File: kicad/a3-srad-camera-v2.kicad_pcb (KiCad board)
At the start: 4 copper layers, 50 x 50 mm, 162 parts, among them J1 BOARD_IND, J2 OUT, J3 Amphenol F32Q 1x22 P=0.5mm, SW1 PWRON, U1 AMS1117-3.3, U2 TPS6521905RHBR, U3 STM32U575RGT6, U4 RV1106G2

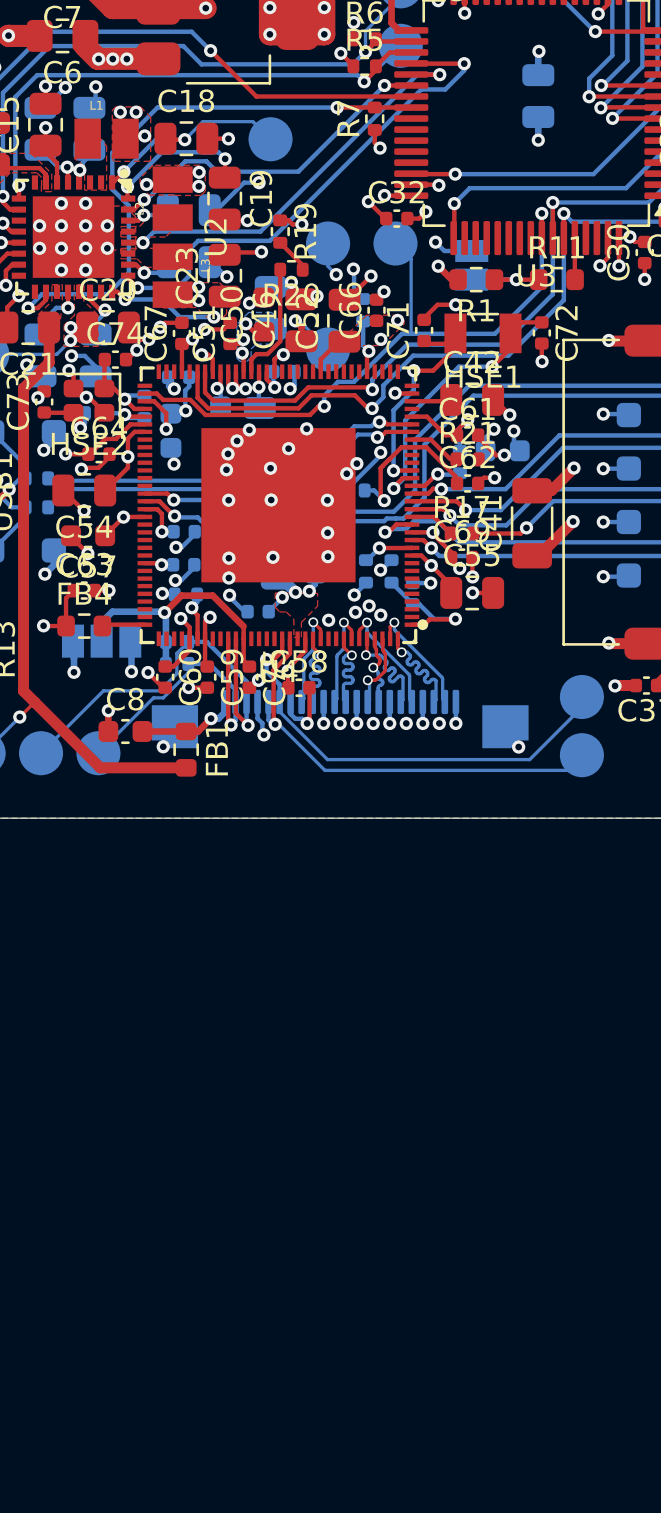
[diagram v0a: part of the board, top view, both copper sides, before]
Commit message: PCB before switching STM32
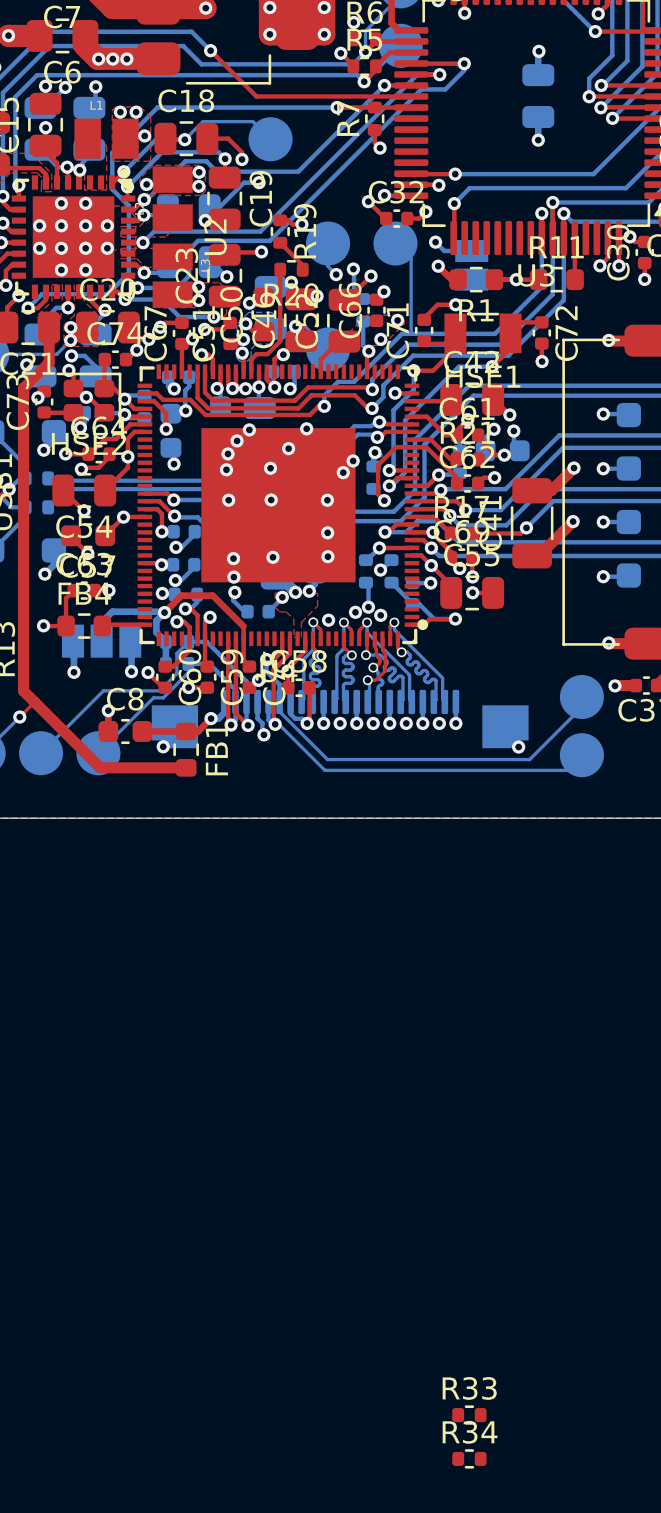
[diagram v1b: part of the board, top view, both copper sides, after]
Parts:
- added R33: DNP, Resistor_SMD:R_0402_1005Metric, F.Cu at (158.0, 153.1)
- added R34: DNP, Resistor_SMD:R_0402_1005Metric, F.Cu at (158.0, 155.1)
- R14, R15: value 22R -> 2.2R
- moved R22 1.08 mm to (153.6, 110.5), turned to 90 degrees
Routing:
- net /VCC_1V8_RK: track 21.8 -> 20.2 mm
- net GND: track 142.7 -> 144.2 mm, vias 158 -> 157
- net Net-(U4A-ETH_EXTR): track 2.22 -> 2.75 mm

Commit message: Add missing passives and microphone
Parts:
- removed the C34 at (159.4, 86.2)
- removed the R21 at (157.9, 109.7)
- added C59: 100nF, Capacitor_SMD:C_0402_1005Metric, F.Cu at (159.3, 109.8)
- added C73: 100nF, Capacitor_SMD:C_0402_1005Metric, B.Cu at (168.3, 101.9)
- added C74: 100nF, Capacitor_SMD:C_0402_1005Metric, B.Cu at (166.7, 101.9)
- added C80: 1uF, Capacitor_SMD:C_0603_1608Metric, F.Cu at (157.6, 102.0)
- added C81: 100nF, Capacitor_SMD:C_0402_1005Metric, F.Cu at (169.4, 99.6)
- added C82: 100pF, Capacitor_SMD:C_0402_1005Metric, B.Cu at (172.3, 101.5)
- added C83: 100pF, Capacitor_SMD:C_0402_1005Metric, B.Cu at (171.3, 100.5)
- added C84: 100pF, Capacitor_SMD:C_0402_1005Metric, B.Cu at (171.3, 102.5)
- added C85: 1uF, Capacitor_SMD:C_0603_1608Metric, F.Cu at (155.3, 101.2)
- added MIC1: IM73A135V01, Sensor_Audio:Infineon_PG-LLGA-5-2, F.Cu at (173.1, 101.5)
- added R19: 10k, Resistor_SMD:R_0603_1608Metric, B.Cu at (136.5, 117.9)
- added R22: 10k, Resistor_SMD:R_0603_1608Metric, B.Cu at (135.0, 117.9)
- added R32: 10k, Resistor_SMD:R_0603_1608Metric, B.Cu at (168.3, 104.4)
- added R33: 10k, Resistor_SMD:R_0603_1608Metric, B.Cu at (166.7, 104.4)
- added R39: 22k, Resistor_SMD:R_0402_1005Metric, F.Cu at (169.5, 101.2)
- added R40: 22k, Resistor_SMD:R_0402_1005Metric, F.Cu at (169.5, 102.1)
- added TP14: TestPoint, a3-srad-camera-v2:TestPoint_Pad_D2.0mm_Small_Courtyard, B.Cu at (170.7, 104.9)
- C38: renamed from C39; moved to B.Cu
- C39: renamed from C40; moved to B.Cu
- C62, R1, R11: moved to B.Cu
- R25: renamed from R33; moved to B.Cu
- R26: renamed from R34; moved to B.Cu
- U3: value STM32U575RGT6 -> STM32U073R8Tx
- moved R26 51.9 mm to (163.8, 103.5), turned to 180 degrees
- moved R25 50.9 mm to (163.8, 102.5), turned to 180 degrees
- moved C39 17.5 mm to (160.2, 117.7)
- moved C38 17.5 mm to (164.0, 117.7)
- moved C62 5.67 mm to (152.2, 111.1), turned to 180 degrees
- moved R11 2.33 mm to (160.2, 100.0), turned to 90 degrees
- moved C65 1.63 mm to (159.8, 107.7)
- moved JP1 0.96 mm to (158.1, 100.0)
- moved C66 0.95 mm to (156.6, 104.5), turned to -90 degrees
- moved C61 0.90 mm to (157.3, 107.9)
- moved R27 0.83 mm to (156.7, 109.6)
- moved R1 0.83 mm to (158.0, 102.3)
- moved C30 0.61 mm to (166.3, 99.9), turned to 180 degrees
- moved HSE1 0.59 mm to (159.1, 104.2)
- moved C41 0.53 mm to (158.1, 106.5)
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- renumbered C35 to C34, C36 to C35, C37 to C36, C38 to C37, C41 to C40, C42 to C41, C43 to C42, C44 to C43, C45 to C44, C46 to C45, C47 to C46, C48 to C47, C49 to C48, C50 to C49, C51 to C50, C52 to C51, C53 to C52, C54 to C53, C55 to C54, C56 to C55, C57 to C56, C58 to C57, C59 to C58, C8 to C6, C64 to C63, C63 to C64, C71 to C66, C72 to C67, C67 to C69, C6 to C7, C73 to C70, C74 to C71, C70 to C72, C66 to C75, C69 to C76, C75 to C77, C76 to C78, C77 to C79, C7 to C8, J3 to J1, J1 to J2, J2 to J3, R19 to R20, R20 to R21, R22 to R23, R23 to R24, R24 to R27, R27 to R28, R28 to R29, R25 to R30, R26 to R31, R32 to R34, R29 to R35, R30 to R36, R31 to R37, TP6 to TP10, TP13 to TP11, TP14 to TP12, TP7 to TP13, TP8 to TP15, TP15 to TP16, TP9 to TP2, TP2 to TP3, TP10 to TP4, TP3 to TP5, TP4 to TP6, TP11 to TP7, TP5 to TP8, TP12 to TP9
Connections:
- C33 pad 1: GND -> /NRST
- C33 pad 2: /NRST -> GND
- U3 pad 30: Net-(U3-VCAP) -> unconnected-(U3-PB11-Pad30)
- U4 pad 22: unconnected-(U4C-SARADC_IN1/PWM1_M1/GPI4_C1_z-Pad22) -> Net-(U4C-SARADC_IN1/PWM1_M1/GPI4_C1_z)
- U4 pad 23: unconnected-(U4C-SARADC_IN0/GPI4_C0_z-Pad23) -> /SOC_RECOVER
- U4 pad 25: Net-(U4A-USB_VBUSDET) -> /RV1106G2 SoC/USB_VBUSDET
- U4 pad 32: unconnected-(U4A-CODEC_MICBIAS-Pad32) -> /RV1106G2 SoC/VCC1V8_MICBIAS
- U4 pad 33: unconnected-(U4A-CODEC_MIC0N-Pad33) -> Net-(U4A-CODEC_MIC0N)
- U4 pad 34: unconnected-(U4A-CODEC_MIC0P-Pad34) -> Net-(U4A-CODEC_MIC0P)
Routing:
- net /RV1106G2 SoC/USB_VBUSDET: track 0.00 -> 47.5 mm, vias 0 -> 1
- net /SOC_RECOVER: track 0.00 -> 24.4 mm, vias 0 -> 3
- net /RV1106G2 SoC/VCC1V8_MICBIAS: track 0.00 -> 22.6 mm, vias 0 -> 2
- net /VCC_1V8_RK: track 20.2 -> 40.3 mm, vias 13 -> 14
- net Net-(U4C-SARADC_IN1/PWM1_M1/GPI4_C1_z): track 0.00 -> 20.0 mm, vias 0 -> 3
- net /RV1106G2 SoC/CODEC_MIC0P: track 0.00 -> 14.6 mm
- net /RV1106G2 SoC/CODEC_MIC0N: track 0.00 -> 10.8 mm
- net GND: track 144.2 -> 154.3 mm, vias 157 -> 164
- net VBUS_5V: track 2.50 -> 7.56 mm
- net /nRESET_SOC: track 30.0 -> 34.6 mm, vias 2 -> 3
- net Net-(U4A-CODEC_MIC0N): track 0.00 -> 4.59 mm
- net Net-(U3-PF3): track 1.89 -> 6.47 mm, vias 0 -> 1
- net Net-(U4A-CODEC_MIC0P): track 0.00 -> 4.12 mm
- net Net-(MIC1-OUT+): track 0.00 -> 3.68 mm, vias 0 -> 1
- net Net-(MIC1-OUT-): track 0.00 -> 3.56 mm, vias 0 -> 1
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- added copper zone on In1.Cu, net GND
